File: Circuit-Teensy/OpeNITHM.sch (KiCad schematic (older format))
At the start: 19 parts, among them J1 Conn_01x14, J2 Conn_01x14, J3 Conn_01x08, J4 Conn_01x11, J5 Conn_01x08, J6 Conn_01x11, J7 Conn_02x08_Odd_Even, J8 Conn_02x08_Odd_Even, J9 Conn_01x05

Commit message: Serial Plot is now normalized, updated schematic for 51k recommendation
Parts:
- R20, R21, R22, R23, R24, R25: value 10k -> 51k
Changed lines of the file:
@@
 P 1900 6250
 F 0 "R20" H 1750 6300 50  0000 C CNN
-F 1 "10k" H 1750 6200 50  0000 C CNN
+F 1 "51k" H 1750 6200 50  0000 C CNN
 F 2 "Resistor_THT:R_Axial_DIN0204_L3.6mm_D1.6mm_P5.08mm_Horizontal" V 1830 6250 50  0001 C CNN
 F 3 "~" H 1900 6250 50  0001 C CNN
@@
 P 2350 6250
 F 0 "R21" H 2200 6300 50  0000 C CNN
-F 1 "10k" H 2200 6200 50  0000 C CNN
+F 1 "51k" H 2200 6200 50  0000 C CNN
 F 2 "Resistor_THT:R_Axial_DIN0204_L3.6mm_D1.6mm_P5.08mm_Horizontal" V 2280 6250 50  0001 C CNN
 F 3 "~" H 2350 6250 50  0001 C CNN
@@
 P 2800 6250
 F 0 "R22" H 2650 6300 50  0000 C CNN
-F 1 "10k" H 2650 6200 50  0000 C CNN
+F 1 "51k" H 2650 6200 50  0000 C CNN
 F 2 "Resistor_THT:R_Axial_DIN0204_L3.6mm_D1.6mm_P5.08mm_Horizontal" V 2730 6250 50  0001 C CNN
 F 3 "~" H 2800 6250 50  0001 C CNN
@@
 P 3250 6250
 F 0 "R23" H 3100 6300 50  0000 C CNN
-F 1 "10k" H 3100 6200 50  0000 C CNN
+F 1 "51k" H 3100 6200 50  0000 C CNN
 F 2 "Resistor_THT:R_Axial_DIN0204_L3.6mm_D1.6mm_P5.08mm_Horizontal" V 3180 6250 50  0001 C CNN
 F 3 "~" H 3250 6250 50  0001 C CNN
@@
 P 3700 6250
 F 0 "R24" H 3550 6300 50  0000 C CNN
-F 1 "10k" H 3550 6200 50  0000 C CNN
+F 1 "51k" H 3550 6200 50  0000 C CNN
 F 2 "Resistor_THT:R_Axial_DIN0204_L3.6mm_D1.6mm_P5.08mm_Horizontal" V 3630 6250 50  0001 C CNN
 F 3 "~" H 3700 6250 50  0001 C CNN
@@
 P 4150 6250
 F 0 "R25" H 4000 6300 50  0000 C CNN
-F 1 "10k" H 4000 6200 50  0000 C CNN
+F 1 "51k" H 4000 6200 50  0000 C CNN
 F 2 "Resistor_THT:R_Axial_DIN0204_L3.6mm_D1.6mm_P5.08mm_Horizontal" V 4080 6250 50  0001 C CNN
 F 3 "~" H 4150 6250 50  0001 C CNN
@@
 Text Notes 800  1650 0    39   ~ 0
 RGB lighting
-Wire Notes Line rgb(181, 36, 194)
+Wire Notes Line rgb(181, 36, 0)
 	1500 1900 1000 1900
-Wire Notes Line rgb(181, 36, 194)
+Wire Notes Line rgb(181, 36, 0)
 	1000 1850 1000 1900
 Wire Notes Line rgb(194, 0, 0)
@@
 Text Notes 800  1850 0    39   ~ 0
 IR LEDs
-Wire Notes Line rgb(181, 36, 194)
+Wire Notes Line rgb(181, 36, 0)
 	3450 1800 2950 1800
-Wire Notes Line rgb(181, 36, 194)
+Wire Notes Line rgb(181, 36, 0)
 	2950 1750 2950 1800
 Text Notes 2750 1750 0    39   ~ 0
 IR LEDs
-Wire Notes Line rgb(181, 36, 194)
+Wire Notes Line rgb(181, 36, 0)
 	3450 2300 3300 2300
-Wire Notes Line rgb(181, 36, 194)
+Wire Notes Line rgb(181, 36, 0)
 	3300 2300 3300 1800
 Wire Notes Line rgb(194, 0, 0)

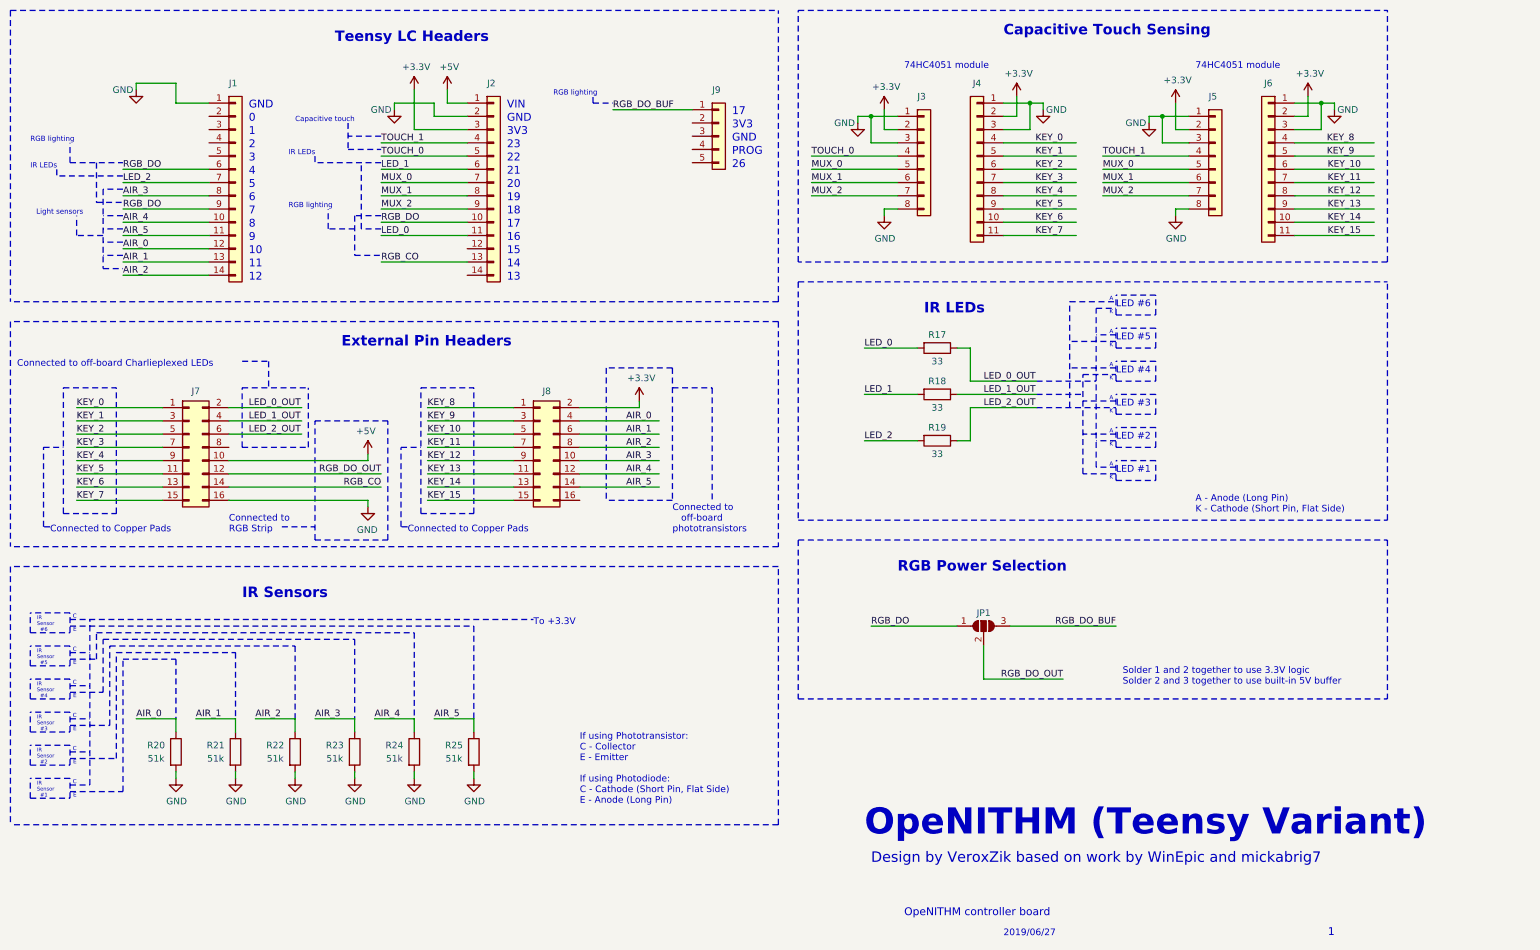
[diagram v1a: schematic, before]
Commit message: Updated main OpeNITHM board to v1.1
Code has not been updated yet, do not use
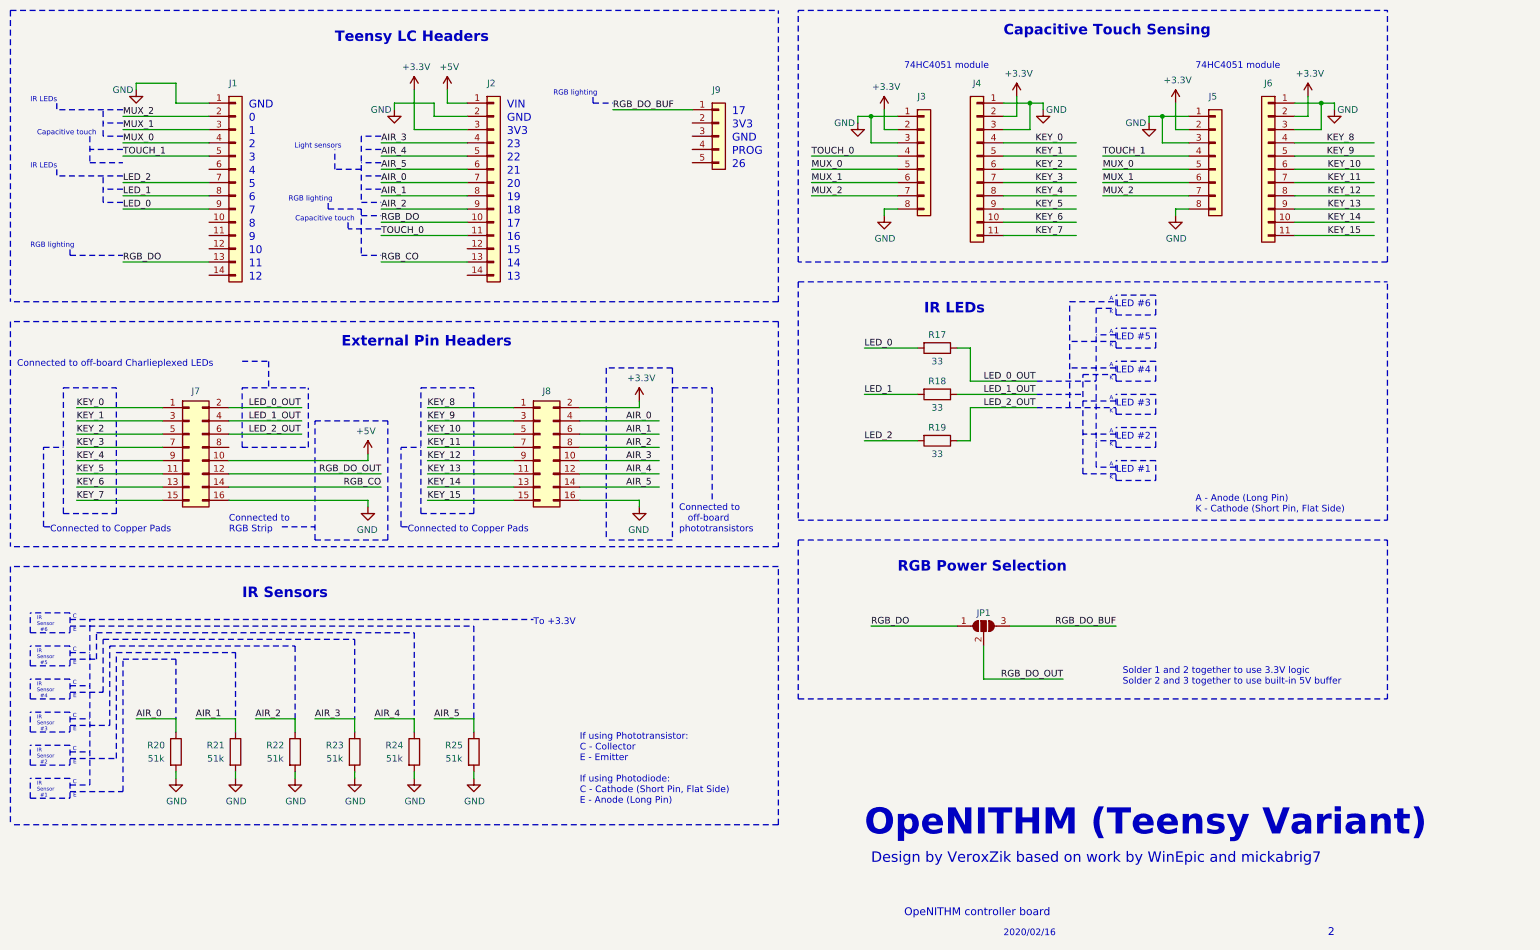
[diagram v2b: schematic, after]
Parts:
- R17, R18, R19: footprint Resistor_THT:R_Axial_DIN0204_L3.6mm_D1.6mm_P5.08mm_Horizontal -> Resistor_THT:R_Axial_DIN0207_L6.3mm_D2.5mm_P7.62mm_Horizontal
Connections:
- wire segments 152 -> 153
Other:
- note added: "2020/02/16"
- note removed: "2019/06/27"
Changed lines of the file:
@@
 EESchema Schematic File Version 4
-LIBS:OpeNITHM-cache
-EELAYER 26 0
+EELAYER 30 0
 EELAYER END
 $Descr A4 11693 8268
@@
 Teensy LC Headers
 Wire Notes Line rgb(194, 0, 0)
-	3450 2200 3250 2200
-Wire Notes Line rgb(194, 0, 0)
-	3250 2200 3250 2500
-Wire Notes Line rgb(194, 0, 0)
-	3250 2500 3450 2500
-Wire Notes Line rgb(194, 0, 0)
-	3250 2300 3050 2300
-Wire Notes Line rgb(194, 0, 0)
-	3050 2300 3050 2150
-Text Notes 2750 2150 0    39   ~ 0
+	3300 2150 3300 2500
+Wire Notes Line rgb(194, 0, 0)
+	3300 2500 3450 2500
+Wire Notes Line rgb(194, 0, 0)
+	3050 2150 3050 2100
+Text Notes 2750 2100 0    39   ~ 0
 RGB lighting
 $Comp
@@
 AIR_0
 Text Notes 8150 7650 0    50   ~ 0
-2019/06/27
+2020/02/16
 Text Notes 7400 7500 0    59   ~ 0
 OpeNITHM controller board
 Text Notes 10600 7650 0    59   ~ 0
-1
+2
 Text Notes 7100 6900 0    197  ~ 39
 OpeNITHM (Teensy Variant)
@@
 Text Label 3850 6000 0    50   ~ 0
 AIR_5
-Text Notes 5650 4600 0    50   ~ 0
+Text Notes 5700 4600 0    50   ~ 0
  Connected to\n   off-board\nphototransistors
 Text Notes 2400 5100 0    79   ~ 16
@@
 F 0 "R17" V 7550 3200 50  0000 C CNN
 F 1 "33" V 7750 3200 50  0000 C CNN
-F 2 "Resistor_THT:R_Axial_DIN0204_L3.6mm_D1.6mm_P5.08mm_Horizontal" V 7580 3200 50  0001 C CNN
+F 2 "Resistor_THT:R_Axial_DIN0207_L6.3mm_D2.5mm_P7.62mm_Horizontal" V 7580 3200 50  0001 C CNN
 F 3 "~" H 7650 3200 50  0001 C CNN
 	1    7650 3200
@@
 F 0 "R18" V 7550 3550 50  0000 C CNN
 F 1 "33" V 7750 3550 50  0000 C CNN
-F 2 "Resistor_THT:R_Axial_DIN0204_L3.6mm_D1.6mm_P5.08mm_Horizontal" V 7580 3550 50  0001 C CNN
+F 2 "Resistor_THT:R_Axial_DIN0207_L6.3mm_D2.5mm_P7.62mm_Horizontal" V 7580 3550 50  0001 C CNN
 F 3 "~" H 7650 3550 50  0001 C CNN
 	1    7650 3550
@@
 F 0 "R19" V 7550 3900 50  0000 C CNN
 F 1 "33" V 7750 3900 50  0000 C CNN
-F 2 "Resistor_THT:R_Axial_DIN0204_L3.6mm_D1.6mm_P5.08mm_Horizontal" V 7580 3900 50  0001 C CNN
+F 2 "Resistor_THT:R_Axial_DIN0207_L6.3mm_D2.5mm_P7.62mm_Horizontal" V 7580 3900 50  0001 C CNN
 F 3 "~" H 7650 3900 50  0001 C CNN
 	1    7650 3900
@@
 Wire Wire Line
 	1150 4350 1800 4350
-Text Label 3450 1750 0    50   ~ 0
+Text Label 3450 2350 0    50   ~ 0
 TOUCH_0
 Wire Wire Line
-	3450 1750 4100 1750
+	3450 2350 4100 2350
 Wire Wire Line
 	3800 3650 4450 3650
@@
 	2850 3750 2300 3750
 Wire Wire Line
-	4100 1850 3450 1850
-Text Label 3450 1850 0    50   ~ 0
+	2150 2050 1500 2050
+Text Label 1500 2050 0    50   ~ 0
 LED_1
 Wire Wire Line
-	3450 2350 4100 2350
-Text Label 3450 2350 0    50   ~ 0
+	1500 2150 2150 2150
+Text Label 1500 2150 0    50   ~ 0
 LED_0
-Text Label 3450 1950 0    50   ~ 0
-MUX_0
-Text Label 3450 2050 0    50   ~ 0
-MUX_1
-Text Label 3450 2150 0    50   ~ 0
+Text Label 1500 1450 0    50   ~ 0
 MUX_2
 Wire Wire Line
-	3450 1950 4100 1950
-Wire Wire Line
-	4100 2050 3450 2050
-Wire Wire Line
-	3450 2150 4100 2150
+	2150 1550 1500 1550
+Wire Wire Line
+	1500 1450 2150 1450
 Text Notes 4400 2700 0    59   ~ 0
 13
@@
 Wire Wire Line
 	3450 2550 4100 2550
-Text Label 1500 2150 0    50   ~ 0
+Text Label 1500 2550 0    50   ~ 0
 RGB_DO
 Wire Wire Line
-	1500 2150 2150 2150
-Wire Wire Line
-	1500 2450 2150 2450
-Wire Wire Line
 	1500 2550 2150 2550
 Wire Wire Line
-	1500 2050 2150 2050
-Wire Wire Line
-	1500 2350 2150 2350
-Wire Wire Line
-	1500 2650 2150 2650
-Wire Wire Line
-	1500 2250 2150 2250
-Text Label 1500 2450 0    50   ~ 0
+	3450 1950 4100 1950
+Wire Wire Line
+	3450 2050 4100 2050
+Wire Wire Line
+	3450 1650 4100 1650
+Wire Wire Line
+	3450 1850 4100 1850
+Wire Wire Line
+	3450 2150 4100 2150
+Wire Wire Line
+	3450 1750 4100 1750
+Text Label 3450 1950 0    50   ~ 0
 AIR_0
-Text Label 1500 2550 0    50   ~ 0
+Text Label 3450 2050 0    50   ~ 0
 AIR_1
-Text Label 1500 2650 0    50   ~ 0
+Text Label 3450 2150 0    50   ~ 0
 AIR_2
-Text Label 1500 2050 0    50   ~ 0
+Text Label 3450 1650 0    50   ~ 0
 AIR_3
-Text Label 1500 2250 0    50   ~ 0
+Text Label 3450 1750 0    50   ~ 0
 AIR_4
-Text Label 1500 2350 0    50   ~ 0
+Text Label 3450 1850 0    50   ~ 0
 AIR_5
-Text Label 1500 1850 0    50   ~ 0
-RGB_DO
-Wire Wire Line
-	1500 1850 2150 1850
 Wire Wire Line
 	1500 1950 2150 1950
@@
 	1900 5550 1900 6000
 Wire Notes Line
-	3450 1600 3200 1600
-Text Notes 3250 1500 2    39   ~ 0
+	1500 1700 1250 1700
+Text Notes 1300 1600 2    39   ~ 0
 Capacitive touch
 Wire Notes Line
-	3200 1700 3450 1700
-Wire Notes Line
-	3200 1500 3200 1700
-Wire Notes Line
-	1500 2000 1350 2000
-Wire Notes Line
-	1350 2000 1350 2600
-Wire Notes Line
-	1350 2600 1500 2600
-Wire Notes Line
-	1500 2500 1350 2500
-Wire Notes Line
-	1500 2400 1350 2400
-Wire Notes Line
-	1500 2300 1350 2300
-Wire Notes Line
-	1500 2200 1350 2200
-Wire Notes Line
-	1350 2350 1150 2350
-Wire Notes Line
-	1150 2350 1150 2200
-Text Notes 1200 2200 2    39   ~ 0
-Light sensors
+	1250 1800 1500 1800
+Wire Notes Line
+	1250 1600 1250 1800
 Wire Wire Line
 	7250 1550 7250 1400
@@
 	7150 5300 7800 5300
 Wire Wire Line
-	4100 1650 3450 1650
-Text Label 3450 1650 0    50   ~ 0
+	2150 1750 1500 1750
+Text Label 1500 1750 0    50   ~ 0
 TOUCH_1
-Wire Notes Line rgb(194, 0, 0)
-	1300 1800 1300 2100
-Wire Notes Line rgb(194, 0, 0)
-	1300 2100 1500 2100
-Wire Notes Line rgb(194, 0, 0)
-	1100 1800 1100 1650
-Text Notes 800  1650 0    39   ~ 0
-RGB lighting
 Wire Notes Line rgb(181, 36, 0)
 	1500 1900 1000 1900
 Wire Notes Line rgb(181, 36, 0)
 	1000 1850 1000 1900
-Wire Notes Line rgb(194, 0, 0)
-	1100 1800 1500 1800
+Wire Notes Line rgb(90, 238, 7)
+	1100 2500 1500 2500
 Text Notes 800  1850 0    39   ~ 0
 IR LEDs
 Wire Notes Line rgb(181, 36, 0)
-	3450 1800 2950 1800
+	1500 2100 1350 2100
 Wire Notes Line rgb(181, 36, 0)
-	2950 1750 2950 1800
-Text Notes 2750 1750 0    39   ~ 0
-IR LEDs
-Wire Notes Line rgb(181, 36, 0)
-	3450 2300 3300 2300
-Wire Notes Line rgb(181, 36, 0)
-	3300 2300 3300 1800
+	1350 2100 1350 1900
 Wire Notes Line rgb(194, 0, 0)
 	5050 1350 5050 1300
@@
 	6450 3000 6450 4700
 Wire Notes Line
-	5650 3350 5650 4350
-Wire Notes Line
-	5650 4350 5150 4350
-Wire Notes Line
-	5150 3350 5150 4350
+	5650 3350 5650 4650
+Wire Notes Line
+	5650 4650 5150 4650
+Wire Notes Line
+	5150 3350 5150 4650
 Wire Notes Line
 	5650 3350 5150 3350
@@
 Text Notes 850  6600 0    28   ~ 0
   IR\nSensor\n  #1
+Text Notes 800  2450 0    39   ~ 0
+RGB lighting
+Wire Notes Line rgb(90, 238, 7)
+	1100 2500 1100 2450
+Text Notes 3150 1700 2    39   ~ 0
+Light sensors
+Wire Notes Line
+	3100 1850 3100 1700
+Wire Notes Line
+	3300 1850 3100 1850
+Wire Notes Line
+	3450 1700 3300 1700
+Wire Notes Line
+	3450 1800 3300 1800
+Wire Notes Line
+	3450 1900 3300 1900
+Wire Notes Line
+	3300 2100 3450 2100
+Wire Notes Line
+	3450 1600 3300 1600
+Wire Notes Line
+	3300 1600 3300 2100
+Wire Notes Line
+	3450 2000 3300 2000
+Wire Notes Line rgb(181, 36, 0)
+	1500 2000 1350 2000
+Wire Notes Line rgb(255, 153, 9)
+	1500 1400 1000 1400
+Wire Notes Line rgb(255, 153, 90)
+	1000 1350 1000 1400
+Text Notes 800  1350 0    39   ~ 0
+IR LEDs
+Wire Notes Line rgb(255, 153, 9)
+	1500 1600 1350 1600
+Wire Notes Line rgb(255, 153, 9)
+	1350 1600 1350 1400
+Wire Notes Line rgb(255, 153, 9)
+	1500 1500 1350 1500
+Wire Wire Line
+	1500 1650 2150 1650
+Text Label 1500 1550 0    50   ~ 0
+MUX_1
+Text Label 1500 1650 0    50   ~ 0
+MUX_0
+Wire Notes Line rgb(194, 0, 0)
+	3050 2150 3300 2150
+Text Notes 3250 2250 2    39   ~ 0
+Capacitive touch
+Wire Notes Line rgb(194, 0, 0)
+	3300 2200 3450 2200
+Wire Notes Line rgb(255, 153, 9)
+	3450 2300 3200 2300
+Wire Notes Line rgb(255, 153, 90)
+	3200 2250 3200 2300
+$Comp
+L power:GND #PWR0104
+U 1 1 5E9D5F1A
+P 5400 4400
+F 0 "#PWR0104" H 5400 4150 50  0001 C CNN
+F 1 "GND" H 5405 4227 50  0000 C CNN
+F 2 "" H 5400 4400 50  0001 C CNN
+F 3 "" H 5400 4400 50  0001 C CNN
+	1    5400 4400
+	-1   0    0    -1
+$EndComp
+Wire Wire Line
+	4950 4350 5400 4350
+Wire Wire Line
+	5400 4350 5400 4400
 $EndSCHEMATC
